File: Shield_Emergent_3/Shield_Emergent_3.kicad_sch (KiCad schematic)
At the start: 17 parts, among them J1 USB3_B_Micro, J2 Conn_02x08_Odd_Even, J3 USB3_B_Micro, U3 SP3012-06UTG, U4 SP3012-06UTG, X1 USB_C_24pins

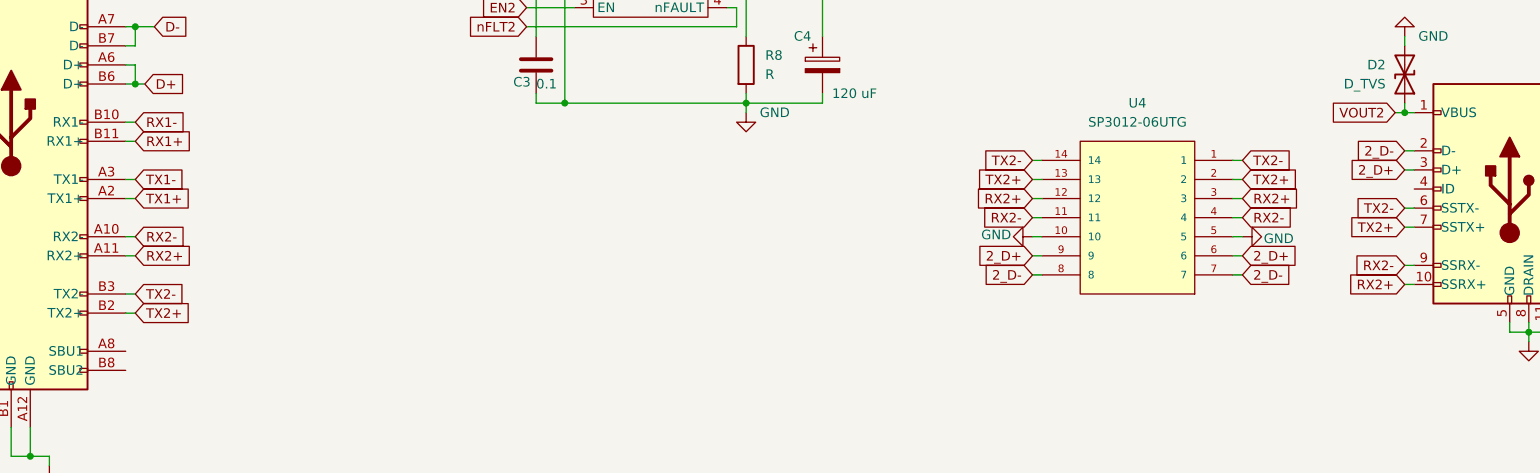
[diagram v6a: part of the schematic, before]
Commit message: v0.8 Partial decomposition was completed
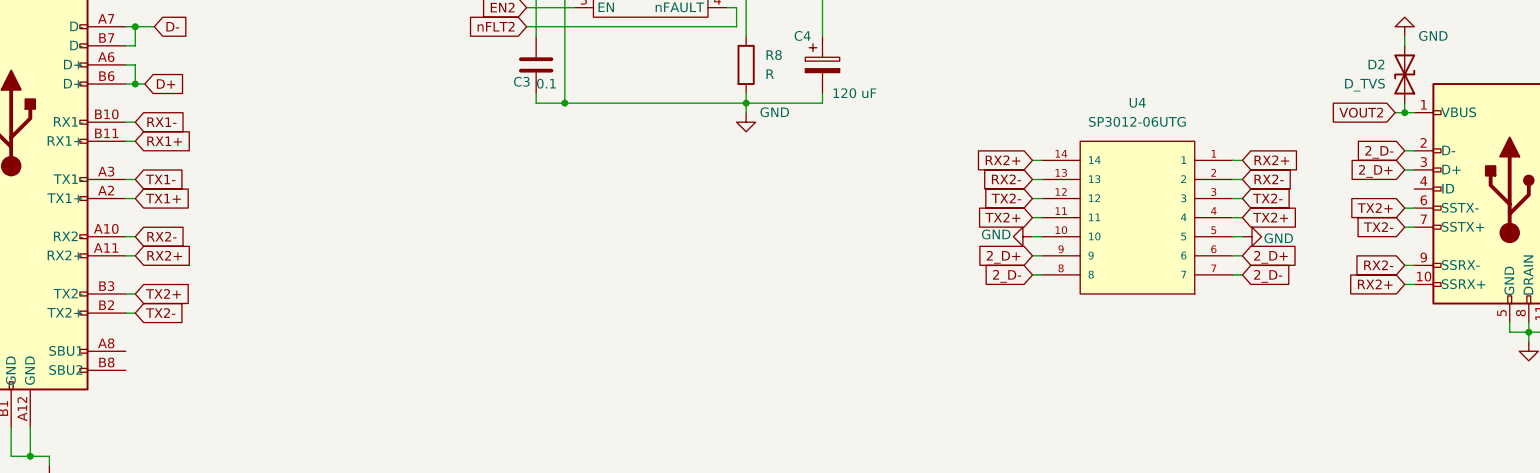
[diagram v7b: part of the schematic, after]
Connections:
- net RX2+: now also U4.1, U4.14; no longer U4.12, U4.3
- net RX2-: now also U4.13, U4.2; no longer U4.11, U4.4
- net TX2+: now also J3.6 (SSTX-), U4.11, U4.4, X1.B3 (TX2-); no longer J3.7 (SSTX+), U4.13, U4.2, X1.B2 (TX2+)
- net TX2-: now also J3.7 (SSTX+), U4.12, U4.3, X1.B2 (TX2+); no longer J3.6 (SSTX-), U4.1, U4.14, X1.B3 (TX2-)

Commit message: v0.9 Decomposition seems 2B completed
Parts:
- removed J2: Conn_02x08_Odd_Even, Connector_PinSocket_2.54mm:PinSocket_2x08_P2.54mm_Vertical, symbol Connector_Generic:Conn_02x08_Odd_Even
- added J2: Conn_02x04_Odd_Even, Connector_PinHeader_2.54mm:PinHeader_2x04_P2.54mm_Vertical, symbol Connector_Generic:Conn_02x04_Odd_Even
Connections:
- net BTN1: now also J2.7 (Pin_7)
- net BTN2: now also J2.8 (Pin_8)
- net EN1: now also J2.3 (Pin_3)
- net EN2: now also J2.4 (Pin_4)
- net VOUT1: now also J2.1 (Pin_1)
- net VOUT2: now also J2.2 (Pin_2)
- net nFLT1: now also J2.5 (Pin_5)
- net nFLT2: now also J2.6 (Pin_6)
